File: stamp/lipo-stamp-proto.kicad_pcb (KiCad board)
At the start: 4 copper layers, 17.8 x 17.8 mm, 31 parts, among them IC1 TP4056, Q1 SI2301CDS-T1-GE3, U1 AP2112K-3.3, U2 AP9101CK6, U3 FS8205

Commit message: Update render
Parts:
- D3, D4: value D_Schottky -> B5819W
- F1: value 2A Polyfuse -> nSMD200

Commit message: Address comments from Henrik
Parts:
- moved R3 2.81 mm to (111.5, 53.7)
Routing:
- net Net-(D2-Pad1): track 11.3 -> 16.1 mm
- net /STAT: track 18.5 -> 21.2 mm, vias 1 -> 2
- net /VMAX: track 18.9 -> 20.7 mm
- net Net-(C1-Pad1): track 28.9 -> 30.3 mm
- net GND: track 3.74 -> 4.52 mm, vias 16 -> 24
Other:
- board text removed: "JLCJLCJLCJLC"

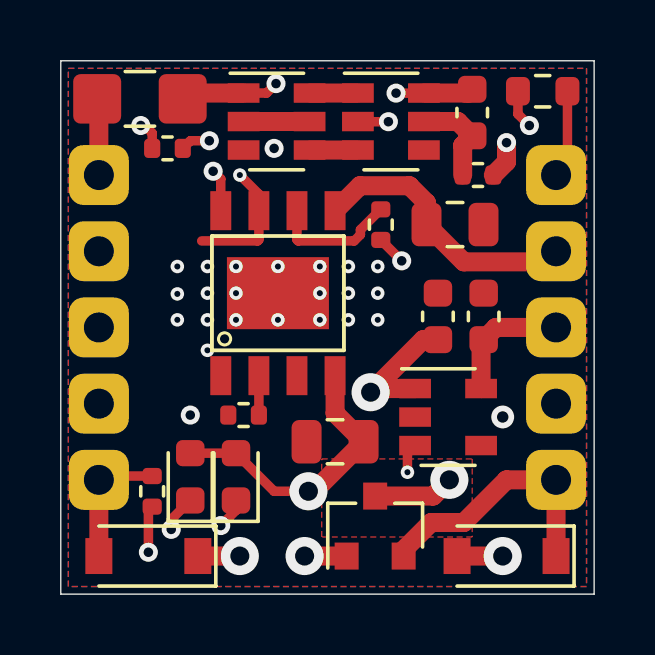
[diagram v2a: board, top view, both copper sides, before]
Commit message: Remove dead trace, increase return path via, add thermal spokes for ground
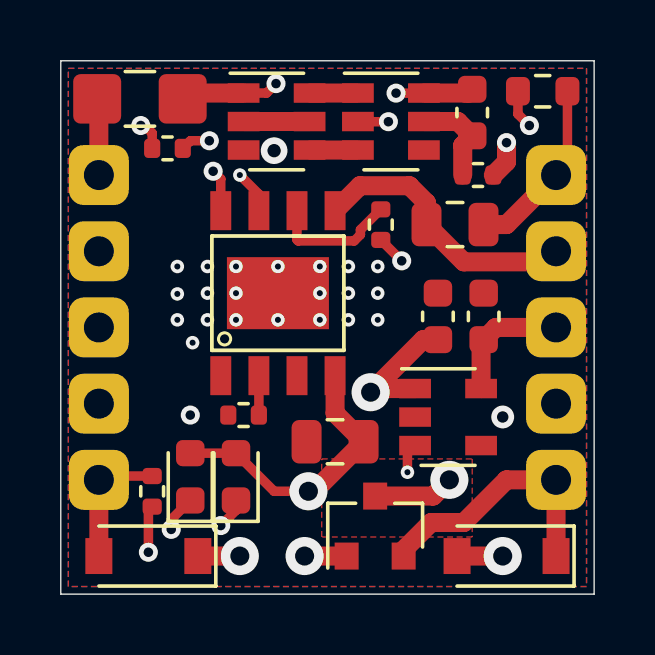
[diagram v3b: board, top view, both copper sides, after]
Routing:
- net GND: track 4.52 -> 7.63 mm
- net /STAT: track 21.2 -> 18.3 mm

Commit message: Rework return path a bit more
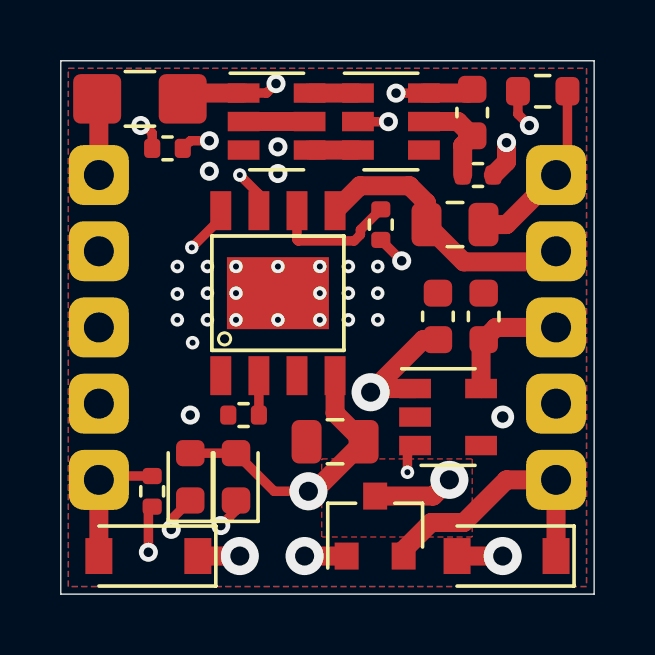
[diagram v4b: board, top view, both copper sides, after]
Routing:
- net Net-(C1-Pad1): track 30.3 -> 27.5 mm
- net GND: vias 24 -> 26
